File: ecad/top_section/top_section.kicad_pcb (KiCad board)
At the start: 2 copper layers, 100 x 87 mm, 129 parts, among them J1 JST PH, J2 JST PH, J3 JST SH, Q1 RE1C002UN, Q10 RE1C002UN, Q2 RE1C002UN, Q3 RE1C002UN, Q4 RE1C002UN, Q5 RE1C002UN, Q6 RE1C002UN, Q7 RE1C002UN, Q8 RE1C002UN, Q9 RE1C002UN, SW1 PEL12T, SW10 PEL12T, SW11 PEL12T, SW12 PEL12T, SW13 PEL12T, SW14 PEL12T, SW15 PEL12T, SW16 SW_Push, SW17 SW_Push, SW18 SW_Push, SW19 SW_Push, SW2 SW_Push, SW20 SW_Push, SW3 PEL12T, SW4 SW_Push, SW5 PEL12T, SW6 SW_Push, SW7 SW_Push, SW8 PEL12T, SW9 SW_Push, U1 TLC5973, U10 TLC5973, U11 MCP23017_ML, U2 TLC5973, U3 TLC5973, U4 TLC5973, U5 TLC5973, U6 TLC5973, U7 TLC5973, U8 TLC5973, U9 TLC5973

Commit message: Updates boards
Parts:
- removed R21, R22, R23, R24, R25, R26: 11k, Resistor_SMD:R_0603_1608Metric
- added JP1: ~, Jumper:SolderJumper-3_P2.0mm_Open_TrianglePad1.0x1.5mm, F.Cu at (79.7, 134.8)
- added JP2: ~, Jumper:SolderJumper-3_P2.0mm_Open_TrianglePad1.0x1.5mm, F.Cu at (77.1, 134.8)
- added JP3: ~, Jumper:SolderJumper-3_P2.0mm_Open_TrianglePad1.0x1.5mm, F.Cu at (74.5, 134.8)
- added R31: 11k, Resistor_SMD:R_0603_1608Metric, B.Cu at (74.0, 133.3)
- added REF**: MountingHole_2.7mm_M2.5, MountingHole:MountingHole_2.7mm_M2.5, F.Cu at (109.5, 92.9)
- J1, J2: footprint Connector_JST:JST_PH_S4B-PH-K_1x04_P2.00mm_Horizontal -> woodpecker:JST_PH_S4B-PH-SM4-TB_1x04-1MP_P2.00mm_Horizontal
- J3: footprint Connector_JST:JST_SH_BM04B-SRSS-TB_1x04-1MP_P1.00mm_Vertical -> woodpecker:JST_SH_BM04B-SRSS-TB_1x04-1MP_P1.00mm_Vertical
- moved R30 44.0 mm to (98.1, 130.5), turned to -90 degrees
- moved J2 8.36 mm to (90.7, 134.1), turned to 180 degrees
- moved J1 5.67 mm to (128.5, 134.2), turned to 180 degrees
- moved R27 3.14 mm to (83.3, 132.5)
- moved REF** 1.00 mm to (53.0, 54.0)
- moved REF** 1.00 mm to (147.0, 54.0)
- moved R28 0.60 mm to (142.1, 133.9)
- moved R29 0.60 mm to (142.1, 132.4)
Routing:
- net /SDOUT: track 58.6 -> 11.1 mm
- net /RotaryEncoder_COL10/SDO: track 45.6 -> 86.3 mm
- net GND: track 888.0 -> 919.1 mm, vias 108 -> 133
- net /3v3_PUP: track 0.00 -> 8.99 mm, vias 0 -> 1
- net /DOUT: track 2.76 -> 11.3 mm
- net +5V: track 646.4 -> 638.3 mm
- net /A2: track 23.4 -> 16.8 mm, vias 2 -> 1
- net /A0: track 16.7 -> 21.7 mm, vias 0 -> 1
- net +3V3: track 18.7 -> 14.0 mm
- net /KeyboardKey_COL1/DIN: track 149.1 -> 144.8 mm
- net /SDIN: track 17.3 -> 14.7 mm
- net /KeyboardKey_COL6/DOUT: track 31.2 -> 33.7 mm
- net /COL3: track 159.3 -> 156.8 mm
- net /A1: track 19.3 -> 20.4 mm, vias 0 -> 1
- net /COL5: track 188.1 -> 187.3 mm
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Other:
- board size 100 x 87 mm -> 100 x 88 mm
- board text added: "Addr"
- board text added: "↑ON"

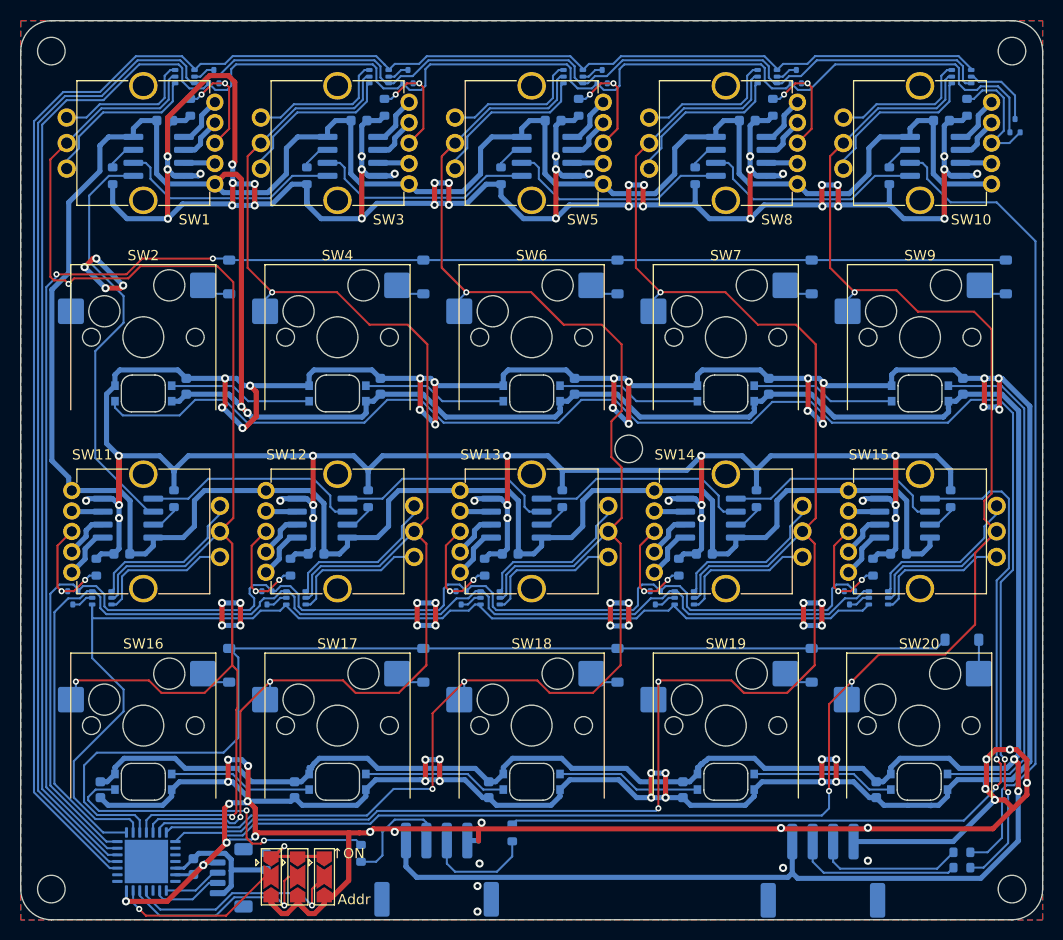
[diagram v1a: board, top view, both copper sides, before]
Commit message: Uses WS2811 led communication everywhere
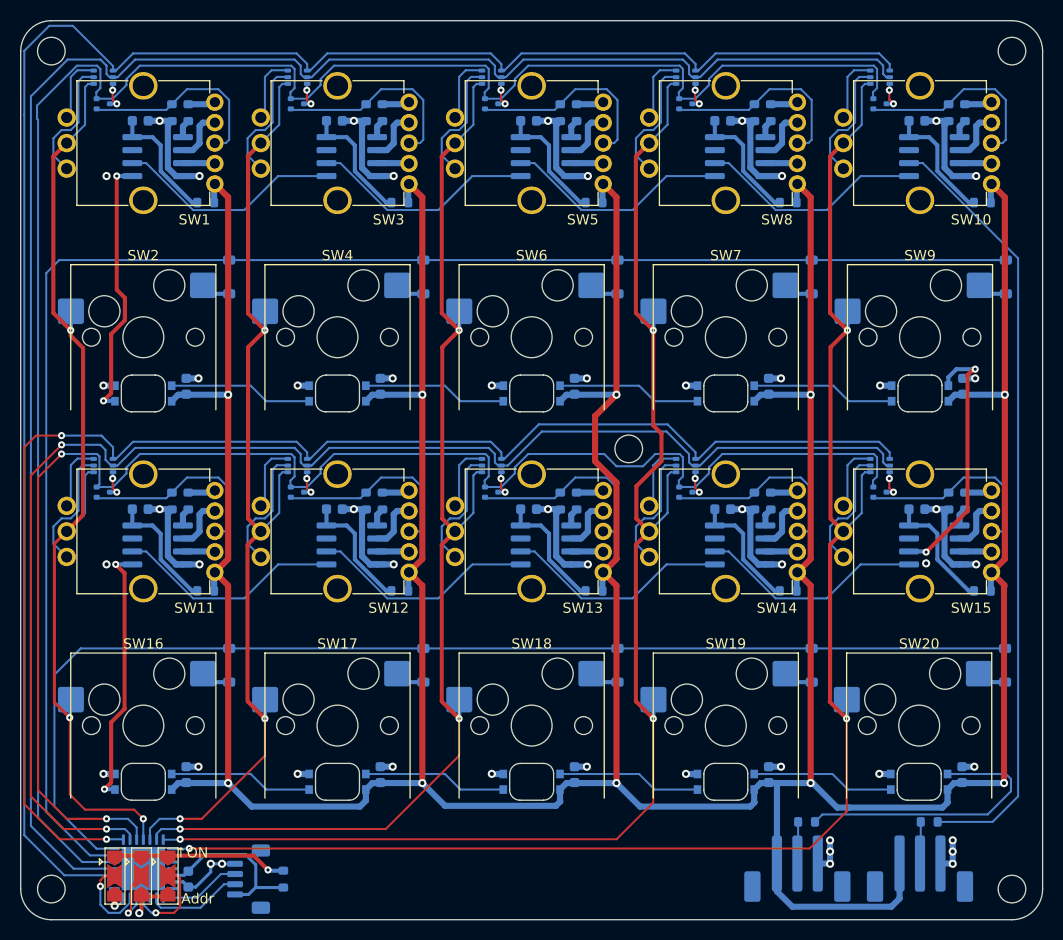
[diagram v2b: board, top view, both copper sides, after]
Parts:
- removed R28, R30: 33, Resistor_SMD:R_0603_1608Metric
- removed U1, U10, U2, U3, U4, U5, U6, U7, U8, U9: TLC5973, Package_SO:SOIC-8_3.9x4.9mm_P1.27mm
- added R21: 68, Resistor_SMD:R_0603_1608Metric, B.Cu at (66.4, 60.0)
- added R22: 68, Resistor_SMD:R_0603_1608Metric, B.Cu at (85.4, 60.0)
- added R23: 68, Resistor_SMD:R_0603_1608Metric, B.Cu at (104.4, 60.0)
- added R24: 68, Resistor_SMD:R_0603_1608Metric, B.Cu at (123.4, 60.0)
- added R25: 68, Resistor_SMD:R_0603_1608Metric, B.Cu at (142.4, 60.0)
- added R26: 68, Resistor_SMD:R_0603_1608Metric, B.Cu at (66.4, 98.0)
- added R32: 68, Resistor_SMD:R_0603_1608Metric, B.Cu at (85.4, 98.0)
- added R33: 68, Resistor_SMD:R_0603_1608Metric, B.Cu at (104.4, 98.0)
- added R34: 68, Resistor_SMD:R_0603_1608Metric, B.Cu at (123.4, 98.0)
- added R35: 68, Resistor_SMD:R_0603_1608Metric, B.Cu at (142.4, 98.0)
- added U12: WS2811, Package_SO:SOIC-8_3.9x4.9mm_P1.27mm, B.Cu at (63.4, 64.3)
- added U13: WS2811, Package_SO:SOIC-8_3.9x4.9mm_P1.27mm, B.Cu at (82.4, 64.3)
- added U14: WS2811, Package_SO:SOIC-8_3.9x4.9mm_P1.27mm, B.Cu at (101.4, 64.3)
- added U15: WS2811, Package_SO:SOIC-8_3.9x4.9mm_P1.27mm, B.Cu at (120.4, 64.3)
- added U16: WS2811, Package_SO:SOIC-8_3.9x4.9mm_P1.27mm, B.Cu at (139.4, 64.3)
- added U17: WS2811, Package_SO:SOIC-8_3.9x4.9mm_P1.27mm, B.Cu at (63.4, 102.3)
- added U18: WS2811, Package_SO:SOIC-8_3.9x4.9mm_P1.27mm, B.Cu at (82.4, 102.3)
- added U19: WS2811, Package_SO:SOIC-8_3.9x4.9mm_P1.27mm, B.Cu at (101.4, 102.3)
- added U20: WS2811, Package_SO:SOIC-8_3.9x4.9mm_P1.27mm, B.Cu at (120.4, 102.3)
- added U21: WS2811, Package_SO:SOIC-8_3.9x4.9mm_P1.27mm, B.Cu at (139.4, 102.3)
- J1, J2: footprint woodpecker:JST_PH_S4B-PH-SM4-TB_1x04-1MP_P2.00mm_Horizontal -> woodpecker:JST_PH_B3B-PH-SM4-TB_1x03-1MP_P2.00mm_Vertical
- R1, R11, R13, R15, R17, R19, R3, R5, R7, R9: value 11k -> 68
- moved R27 43.7 mm to (126.9, 129.4), turned to 0 degrees
- moved J2 35.3 mm to (126.0, 134.0), turned to 0 degrees
- moved JP1 15.3 mm to (64.4, 134.7)
- moved JP2 15.3 mm to (61.8, 134.7)
- moved JP3 15.3 mm to (59.2, 134.7)
- moved Q5 13.4 mm to (134.1, 59.2), turned to 0 degrees
- moved D16 12.9 mm to (58.1, 94.6), turned to 0 degrees
- moved D17 12.9 mm to (77.1, 94.6), turned to 0 degrees
- moved D18 12.9 mm to (96.1, 94.6), turned to 0 degrees
- moved D19 12.9 mm to (115.1, 94.6), turned to 0 degrees
- moved D20 12.9 mm to (134.1, 94.6), turned to 0 degrees
- moved Q1 11.1 mm to (58.1, 59.2), turned to 0 degrees
- moved Q2 11.1 mm to (77.1, 59.2), turned to 0 degrees
- moved Q3 11.1 mm to (96.1, 59.2), turned to 0 degrees
- moved Q4 11.1 mm to (115.1, 59.2), turned to 0 degrees
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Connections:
- C1 pad 1: +5V -> /RotaryEncoder_COL1/+5V_smooth
- C10 pad 1: +5V -> /RotaryEncoder_COL5/+5V_smooth
- C11 pad 1: +5V -> /RotaryEncoder_COL6/+5V_smooth
- C12 pad 1: +5V -> /RotaryEncoder_COL7/+5V_smooth
- C13 pad 1: +5V -> /RotaryEncoder_COL8/+5V_smooth
- C14 pad 1: +5V -> /RotaryEncoder_COL9/+5V_smooth
- C15 pad 1: +5V -> /RotaryEncoder_COL10/+5V_smooth
- C3 pad 1: +5V -> /RotaryEncoder_COL2/+5V_smooth
- C5 pad 1: +5V -> /RotaryEncoder_COL3/+5V_smooth
- C8 pad 1: +5V -> /RotaryEncoder_COL4/+5V_smooth
- D1 pad 1: /RotaryEncoder_COL1/H_QB -> /COL1
- D1 pad 2: /COL1 -> /RotaryEncoder_COL1/H_QB
- D1 pad 5: /RotaryEncoder_COL1/Q_HS -> /R1_QB
- D1 pad 6: /R1_QB -> /RotaryEncoder_COL1/Q_HS
- D12 pad 1: /RotaryEncoder_COL4/H_QB -> /COL4
- D12 pad 2: /COL4 -> /RotaryEncoder_COL4/H_QB
- D12 pad 5: /RotaryEncoder_COL4/Q_HS -> /R1_QB
- D12 pad 6: /R1_QB -> /RotaryEncoder_COL4/Q_HS
- D13 pad 2: /KeyboardKey_COL10/DIN -> /KeyboardKey_COL5/DOUT
- D15 pad 1: /RotaryEncoder_COL5/H_QB -> /COL5
- D15 pad 2: /COL5 -> /RotaryEncoder_COL5/H_QB
- D15 pad 5: /RotaryEncoder_COL5/Q_HS -> /R1_QB
- D15 pad 6: /R1_QB -> /RotaryEncoder_COL5/Q_HS
- D16 pad 1: /RotaryEncoder_COL6/H_QB -> /COL1
- D16 pad 2: /COL1 -> /RotaryEncoder_COL6/H_QB
- D16 pad 5: /RotaryEncoder_COL6/Q_HS -> /R3_QB
- D16 pad 6: /R3_QB -> /RotaryEncoder_COL6/Q_HS
- D17 pad 1: /RotaryEncoder_COL7/H_QB -> /COL2
- D17 pad 2: /COL2 -> /RotaryEncoder_COL7/H_QB
- D17 pad 5: /RotaryEncoder_COL7/Q_HS -> /R3_QB
- D17 pad 6: /R3_QB -> /RotaryEncoder_COL7/Q_HS
- D18 pad 1: /RotaryEncoder_COL8/H_QB -> /COL3
- D18 pad 2: /COL3 -> /RotaryEncoder_COL8/H_QB
- D18 pad 5: /RotaryEncoder_COL8/Q_HS -> /R3_QB
- D18 pad 6: /R3_QB -> /RotaryEncoder_COL8/Q_HS
- D19 pad 1: /RotaryEncoder_COL9/H_QB -> /COL4
- D19 pad 2: /COL4 -> /RotaryEncoder_COL9/H_QB
- D19 pad 5: /RotaryEncoder_COL9/Q_HS -> /R3_QB
- D19 pad 6: /R3_QB -> /RotaryEncoder_COL9/Q_HS
- D20 pad 1: /RotaryEncoder_COL10/H_QB -> /COL5
- D20 pad 2: /COL5 -> /RotaryEncoder_COL10/H_QB
- D20 pad 5: /RotaryEncoder_COL10/Q_HS -> /R3_QB
- D20 pad 6: /R3_QB -> /RotaryEncoder_COL10/Q_HS
- D23 pad 2: /KeyboardKey_COL6/DIN -> /KeyboardKey_COL7/DOUT
- D23 pad 4: /KeyboardKey_COL7/DIN -> /KeyboardKey_COL6/DOUT
- D25 pad 2: /KeyboardKey_COL7/DIN -> /KeyboardKey_COL8/DOUT
- D25 pad 4: /KeyboardKey_COL8/DIN -> /KeyboardKey_COL7/DOUT
- D27 pad 2: /KeyboardKey_COL8/DIN -> /KeyboardKey_COL10/DIN
- D27 pad 4: /KeyboardKey_COL10/DOUT -> /KeyboardKey_COL8/DOUT
- D4 pad 1: /RotaryEncoder_COL2/H_QB -> /COL2
- D4 pad 2: /COL2 -> /RotaryEncoder_COL2/H_QB
- D4 pad 5: /RotaryEncoder_COL2/Q_HS -> /R1_QB
- D4 pad 6: /R1_QB -> /RotaryEncoder_COL2/Q_HS
- D7 pad 1: /RotaryEncoder_COL3/H_QB -> /COL3
- D7 pad 2: /COL3 -> /RotaryEncoder_COL3/H_QB
- D7 pad 5: /RotaryEncoder_COL3/Q_HS -> /R1_QB
- D7 pad 6: /R1_QB -> /RotaryEncoder_COL3/Q_HS
- J1 pad 1: GND -> +5V
- J1 pad 2: /SDIN -> /DIN
- J1 pad 3: /DIN -> GND
- J2 pad 1: GND -> +5V
- J2 pad 2: /SDOUT -> /DOUT
- J2 pad 3: /DOUT -> GND
- R1 pad 1: /RotaryEncoder_COL1/VREF -> +5V
- R1 pad 2: GND -> /RotaryEncoder_COL1/+5V_smooth
- R11 pad 1: /RotaryEncoder_COL6/VREF -> +5V
- R11 pad 2: GND -> /RotaryEncoder_COL6/+5V_smooth
- R13 pad 1: /RotaryEncoder_COL7/VREF -> +5V
- R13 pad 2: GND -> /RotaryEncoder_COL7/+5V_smooth
- R15 pad 1: /RotaryEncoder_COL8/VREF -> +5V
- R15 pad 2: GND -> /RotaryEncoder_COL8/+5V_smooth
- R17 pad 1: /RotaryEncoder_COL9/VREF -> +5V
- R17 pad 2: GND -> /RotaryEncoder_COL9/+5V_smooth
- R19 pad 1: /RotaryEncoder_COL10/VREF -> +5V
- R19 pad 2: GND -> /RotaryEncoder_COL10/+5V_smooth
- R27 pad 2: /KeyboardKey_COL6/DOUT -> /KeyboardKey_COL10/DOUT
- R29 pad 1: /RotaryEncoder_COL5/SDI -> /RotaryEncoder_COL5/DIN
- R29 pad 2: /SDIN -> /DIN
- R3 pad 1: /RotaryEncoder_COL2/VREF -> +5V
- R3 pad 2: GND -> /RotaryEncoder_COL2/+5V_smooth
- R5 pad 1: /RotaryEncoder_COL3/VREF -> +5V
- R5 pad 2: GND -> /RotaryEncoder_COL3/+5V_smooth
- R7 pad 1: /RotaryEncoder_COL4/VREF -> +5V
- R7 pad 2: GND -> /RotaryEncoder_COL4/+5V_smooth
- R9 pad 1: /RotaryEncoder_COL5/VREF -> +5V
- R9 pad 2: GND -> /RotaryEncoder_COL5/+5V_smooth
- U11 pad 21: /R3_SW -> /R4_SW
- U11 pad 22: /R3_QB -> /R3_QA
- U11 pad 23: /R3_QA -> /R3_QB
- U11 pad 24: /R4_SW -> /R3_SW
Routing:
- net GND: track 919.1 -> 149.7 mm, vias 133 -> 53
- net +5V: track 638.3 -> 469.7 mm, vias 4 -> 10
- net /KeyboardKey_COL1/DIN: track 144.8 -> 25.9 mm
- net /RotaryEncoder_COL10/SDO: track 86.3 -> 0.00 mm, vias 2 -> 0
- net /RotaryEncoder_COL5/SDI: track 80.0 -> 0.00 mm
- net /RotaryEncoder_COL5/DIN: track 0.00 -> 76.1 mm
- net /COL1: track 146.9 -> 95.5 mm
- net /COL2: track 139.6 -> 97.0 mm
- net /COL3: track 156.8 -> 115.1 mm
- net /RotaryEncoder_COL1/SDO: track 40.8 -> 0.00 mm
- net /COL4: track 177.0 -> 136.4 mm
- net /KeyboardKey_COL10/DIN: track 50.7 -> 13.9 mm
- net /COL5: track 187.3 -> 154.7 mm
- net /R3_QA: track 111.6 -> 141.3 mm, vias 0 -> 2
- net /R3_SW: track 124.1 -> 151.2 mm, vias 0 -> 2
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- added copper zone on In1.Cu, net GND
- added copper zone on In2.Cu, net GND
- removed copper zone on B.Cu, net GND
- removed copper zone on F.Cu, net GND
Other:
- copper layers 2 -> 4

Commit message: Uses Attiny1617 MCU for ADC & Matrix RO
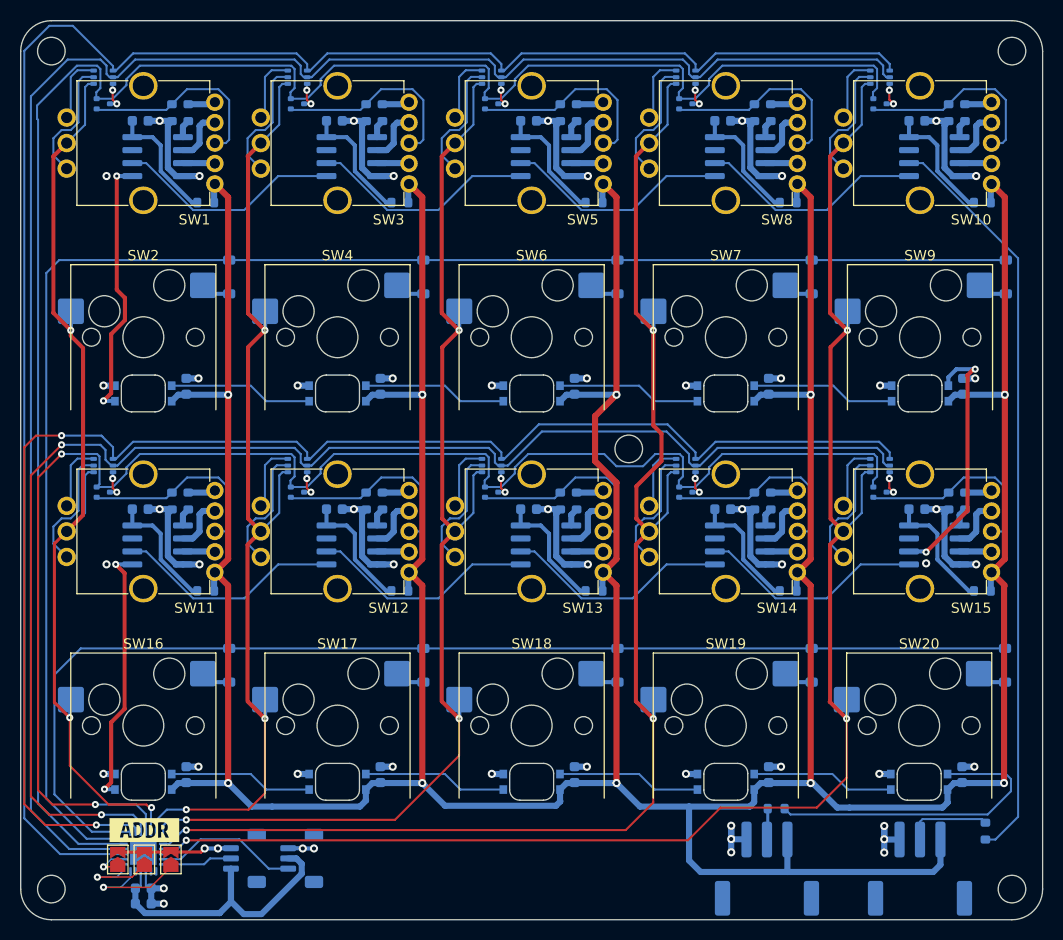
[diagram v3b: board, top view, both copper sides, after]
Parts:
- removed R31: 11k, Resistor_SMD:R_0603_1608Metric
- added C22: 10u, Capacitor_SMD:C_0603_1608Metric, B.Cu at (62.0, 137.4)
- added J4: JST SH, woodpecker:JST_SH_BM03B-SRSS-TB_1x03-1MP_P1.00mm_Vertical, B.Cu at (77.5, 133.0)
- added kibuzzard-68B5BEB6: G***, kibuzzard-68B5BEB6, F.Cu at (62.1, 130.2)
- J1, J2: footprint woodpecker:JST_PH_B3B-PH-SM4-TB_1x03-1MP_P2.00mm_Vertical -> woodpecker:JST_PH_S3B-PH-SM4-TB_1x03-1MP_P2.00mm_Horizontal
- J3: footprint woodpecker:JST_SH_BM04B-SRSS-TB_1x04-1MP_P1.00mm_Vertical -> woodpecker:JST_SH_BM03B-SRSS-TB_1x03-1MP_P1.00mm_Vertical
- JP1, JP2, JP3: value ~ -> SolderJumper_2_Open; footprint Jumper:SolderJumper-3_P2.0mm_Open_TrianglePad1.0x1.5mm -> Jumper:SolderJumper-2_P1.3mm_Open_TrianglePad1.0x1.5mm
- U11: value MCP23017_ML -> ATtiny1617-M; footprint Package_DFN_QFN:QFN-28-1EP_6x6mm_P0.65mm_EP4.25x4.25mm -> Package_DFN_QFN:QFN-24-1EP_4x4mm_P0.5mm_EP2.6x2.6mm
- moved R29 5.57 mm to (144.4, 130.3), turned to 90 degrees
- moved C21 4.49 mm to (62.0, 135.9), turned to 0 degrees
- moved R27 3.25 mm to (123.9, 128.1)
- moved J2 2.97 mm to (123.0, 134.0), turned to 180 degrees
- moved J3 2.06 mm to (71.9, 133.0)
- moved U11 1.68 mm to (62.0, 132.3), turned to 90 degrees
- moved JP2 1.65 mm to (62.1, 133.1), turned to 90 degrees
- moved JP1 1.65 mm to (64.7, 133.1), turned to 90 degrees
- moved JP3 1.65 mm to (59.5, 133.1), turned to 90 degrees
- turned J1 to 180 degrees
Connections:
- J3 pad 2: /SDA -> /TX
- J3 pad 3: /SCK -> GND
- JP1 pad 1: /3v3_PUP -> /A0
- JP1 pad 2: /A0 -> GND
- JP2 pad 1: /3v3_PUP -> /A1
- JP2 pad 2: /A1 -> GND
- JP3 pad 1: /3v3_PUP -> /A2
- JP3 pad 2: /A2 -> GND
- U11 pad 1: /COL5 -> unconnected-(U11-PA2-Pad1)
- U11 pad 10: unconnected-(U11-NC-Pad10) -> /R1_QB
- U11 pad 11: /A0 -> /R1_SW
- U11 pad 12: /A1 -> /R2_SW
- U11 pad 13: /A2 -> /R4_SW
- U11 pad 14: GND -> /R3_QA
- U11 pad 15: unconnected-(U11-INTB-Pad15) -> /R3_QB
- U11 pad 16: unconnected-(U11-INTA-Pad16) -> /R3_SW
- U11 pad 17: /R1_QA -> /COL1
- U11 pad 18: /R1_QB -> /COL2
- U11 pad 19: /R1_SW -> /COL3
- U11 pad 20: /R2_SW -> /COL4
- U11 pad 21: /R4_SW -> /COL5
- U11 pad 22: /R3_QA -> unconnected-(U11-PC5-Pad22)
- U11 pad 23: /R3_QB -> /UDPI
- U11 pad 24: /R3_SW -> /TX
- U11 pad 25: /COL1 -> GND
- U11 pad 3: unconnected-(U11-GPB6-Pad3) -> GND
- U11 pad 4: unconnected-(U11-GPB7-Pad4) -> +3V3
- U11 pad 5: +3V3 -> unconnected-(U11-PA4-Pad5)
- U11 pad 6: GND -> /A0
- U11 pad 7: unconnected-(U11-NC-Pad7) -> /A1
- U11 pad 8: /SCK -> /A2
- U11 pad 9: /SDA -> /R1_QA
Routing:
- net /3v3_PUP: track 17.1 -> 0.00 mm, vias 1 -> 0
- net +3V3: track 16.6 -> 31.9 mm
- net /UDPI: track 0.00 -> 14.2 mm
- net GND: track 149.7 -> 161.1 mm, vias 53 -> 55
- net /SDA: track 9.38 -> 0.00 mm
- net +5V: track 469.7 -> 478.9 mm
- net /SCK: track 7.98 -> 0.00 mm
- net /TX: track 0.00 -> 6.88 mm
- net /A2: track 8.10 -> 3.67 mm
- net /DIN: track 4.11 -> 8.40 mm
- net /KeyboardKey_COL10/DOUT: track 28.0 -> 30.9 mm
- net /RotaryEncoder_COL5/DIN: track 76.1 -> 73.3 mm
- net /A1: track 6.04 -> 8.44 mm
- net /A0: track 8.95 -> 11.1 mm
- net /COL2: track 97.0 -> 98.2 mm
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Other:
- board text removed: "Addr"
- board text removed: "↑ON"

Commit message: [WIP] Control board
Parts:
- added kibuzzard-68C2D93D: G***, kibuzzard-68C2D93D, B.Cu at (130.5, 133.0)
- added kibuzzard-68C2D94D: G***, kibuzzard-68C2D94D, B.Cu at (115.5, 133.2)
- added kibuzzard-68C2D999: G***, kibuzzard-68C2D999, B.Cu at (78.0, 137.5)
- added kibuzzard-68C2D9C3: G***, kibuzzard-68C2D9C3, B.Cu at (72.5, 137.5)
